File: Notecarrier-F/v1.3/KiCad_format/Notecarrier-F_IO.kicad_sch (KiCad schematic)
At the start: 2 parts, among them J10 CES-124-01-S-S, J9 CES-124-01-S-S

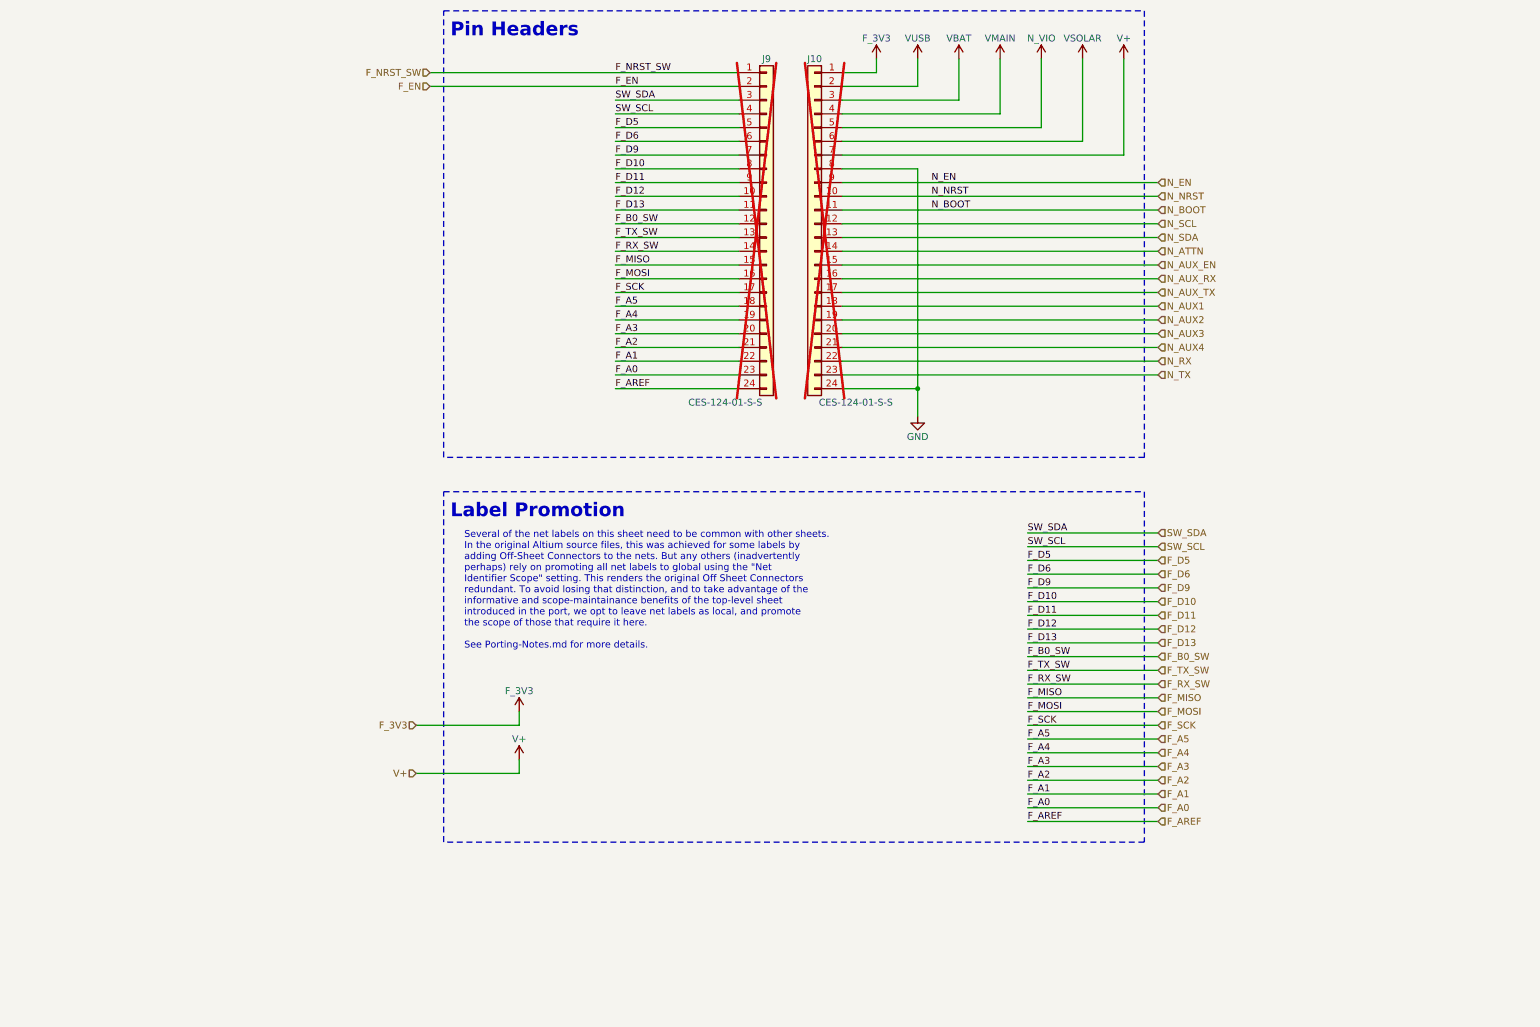
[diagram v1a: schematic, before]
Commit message: Notecarrier-F v1.3: KiCad 9 port from the release-day Altium sources
Replace the hand-made KiCad 7 port (which described v1.2, with a half-applied
v1.3 schematic delta and an ERRATA file) with a direct import of the v1.3
Altium project, recovered from the design archive's history: committed by the
design house on 2023-07-10, the day of the 2200-814 fabrication package, with a
Rev 11 schematic PDF byte-identical to the one published here. The Altium
sources are published alongside as Notecarrier-F/v1.3/Altium, as for v1.5.

The port follows the v1.5 procedure (KiCad 9.0.9 Altium project importer plus
scripted cleanup, scripts kept under documentation/scripts). All validation
gates pass: ERC 0, DRC 0 with schematic parity, BOM exact (94/94 vs
3000-653-002), placement 89/89 vs PNP-3000-653-002, gerber diff exact on outer
copper and masks with the reviewed inner-annulus/silk classes frozen as the
baseline, KiCanvas and RAG. The KiCad netlist was also matched pad by pad
against the nets carried by the Altium board file (0 conflicts).

J9/J10 are fitted per the released BOM (the 2023-08-31 re-save of the project
flips the variant to match); J11/R11/R12 are DNP. Design rules follow the
board's own Altium rule set (0.1 mm clearance). The old hand-port notes are
kept as History_Porting-Notes-hand-port.md because the harness README cites
them for the gerber-diff recipe; the RAG exclusion comment and the product
README are updated accordingly.

Co-Authored-By: Claude Fable 5.1 <noreply@anthropic.com>
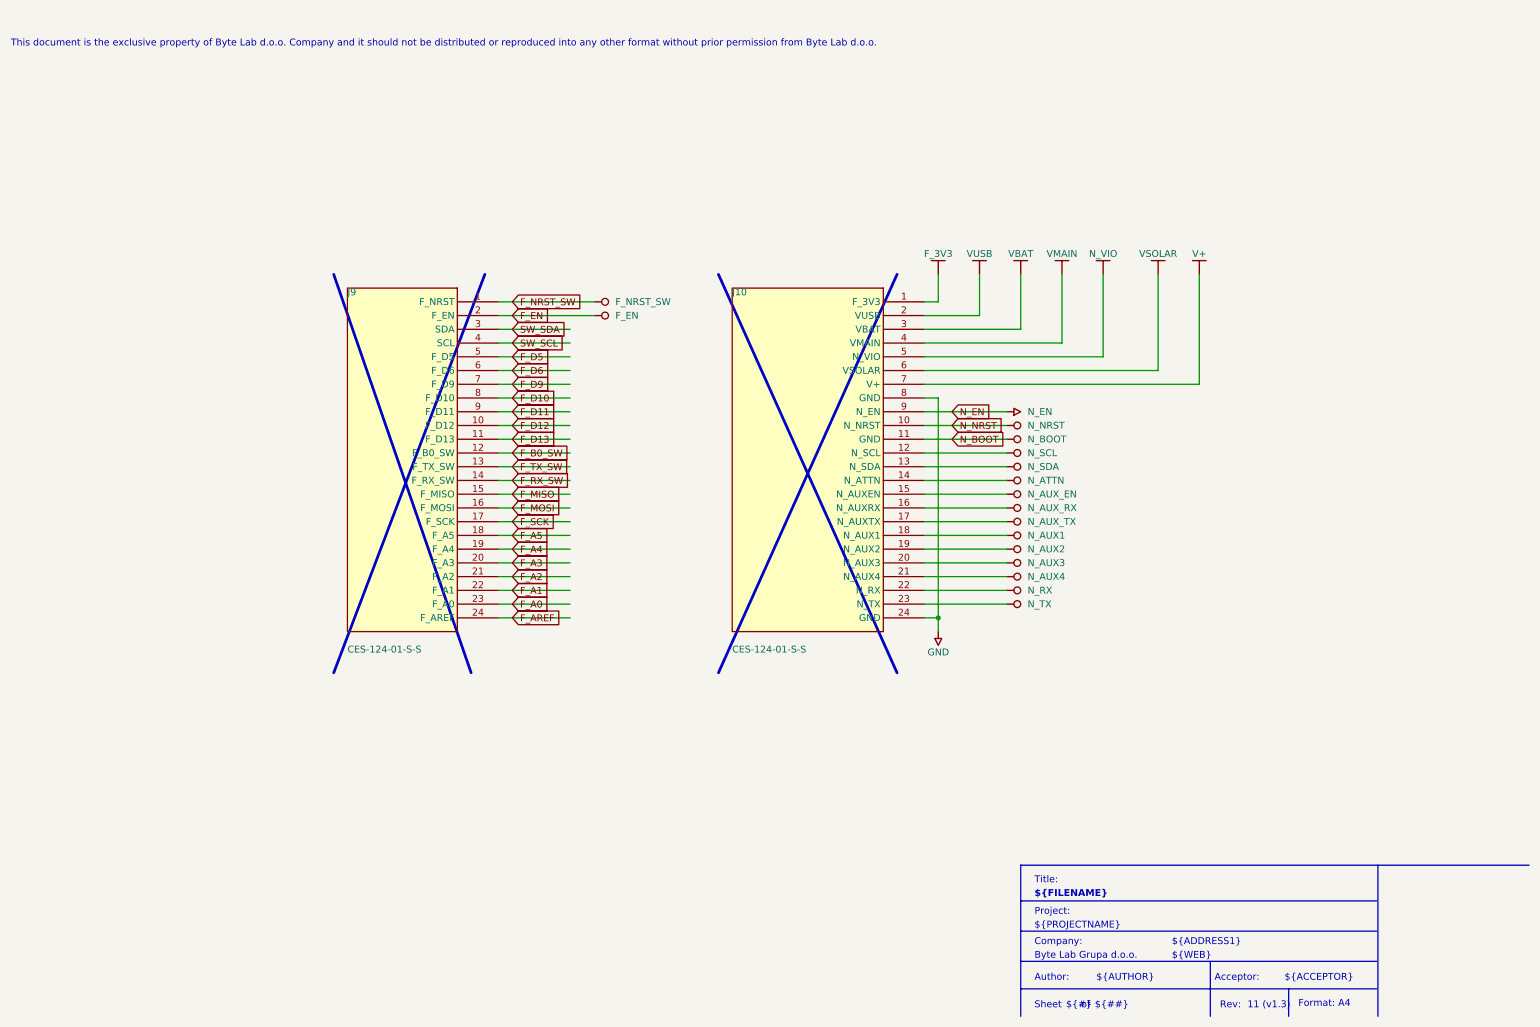
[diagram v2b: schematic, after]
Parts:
- removed J10, J9: CES-124-01-S-S, blues-kicad-lib:CES-124-01-S-S_Fv1.2, symbol Connector_Generic:Conn_01x24
- added J10: CES-124-01-S-S, Notecarrier-F-altium-import:CES-124-01-S-S, symbol n21-p2:root_0_SIDECON_N_n21-p2.SchLib_0
- added J9: CES-124-01-S-S, Notecarrier-F-altium-import:CES-124-01-S-S, symbol n21-p2:root_0_SIDECON_n21-p2.SchLib_0
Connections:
- net F_3V3: now also J10.1 (F_3V3)
- net F_A0: now also J9.23 (F_A0)
- net F_A1: now also J9.22 (F_A1)
- net F_A2: now also J9.21 (F_A2)
- net F_A3: now also J9.20 (F_A3)
- net F_A4: now also J9.19 (F_A4)
- net F_A5: now also J9.18 (F_A5)
- net F_AREF: now also J9.24 (F_AREF)
- net F_B0_SW: now also J9.12 (F_B0_SW)
- net F_D10: now also J9.8 (F_D10)
- net F_D11: now also J9.9 (F_D11)
- net F_D12: now also J9.10 (F_D12)
- net F_D13: now also J9.11 (F_D13)
- net F_D5: now also J9.5 (F_D5)
- net F_D6: now also J9.6 (F_D6)
- net F_D9: now also J9.7 (F_D9)
- net F_EN: now also J9.2 (F_EN)
- net F_MISO: now also J9.15 (F_MISO)
- net F_MOSI: now also J9.16 (F_MOSI)
- net F_NRST_SW: now also J9.1 (F_NRST)
- net F_RX_SW: now also J9.14 (F_RX_SW)
- net F_SCK: now also J9.17 (F_SCK)
- net F_TX_SW: now also J9.13 (F_TX_SW)
- net GND: now also J10.24 (GND), J10.8 (GND)
- net N_ATTN: now also J10.14 (N_ATTN)
- net N_AUX1: now also J10.18 (N_AUX1)
- net N_AUX2: now also J10.19 (N_AUX2)
- net N_AUX3: now also J10.20 (N_AUX3)
- net N_AUX4: now also J10.21 (N_AUX4)
- net N_AUX_EN: now also J10.15 (N_AUXEN)
- net N_AUX_RX: now also J10.16 (N_AUXRX)
- net N_AUX_TX: now also J10.17 (N_AUXTX)
- net N_BOOT: now also J10.11 (GND)
- net N_EN: now also J10.9 (N_EN)
- net N_NRST: now also J10.10 (N_NRST)
- net N_RX: now also J10.22 (N_RX)
- net N_SCL: now also J10.12 (N_SCL)
- net N_SDA: now also J10.13 (N_SDA)
- net N_TX: now also J10.23 (N_TX)
- net N_VIO: now also J10.5 (N_VIO)
- net SW_SCL: now also J9.4 (SCL)
- net SW_SDA: now also J9.3 (SDA)
- net V+: now also J10.7 (V+)
- net VBAT: now also J10.3 (VBAT)
- net VMAIN: now also J10.4 (VMAIN)
- net VSOLAR: now also J10.6 (VSOLAR)
- net VUSB: now also J10.2 (VUSB)
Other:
- note added: "${##}"
- note added: "${#}"
- note added: "${ACCEPTOR}"
- note added: "${ADDRESS1}"
- note added: "${AUTHOR}"
- note added: "${COMPANY}"
- note added: "${FILENAME}"
- note added: "${PROJECTNAME}"
- note added: "${REVISION}"
- note added: "${WEB}"
- note added: "Acceptor:"
- note added: "Author:"
- note added: "Company:"
- note added: "Format: A4"
- note added: "Project:"
- note added: "Rev:"
- note added: "Sheet"
- note added: "This document is the exclusive property of Byte Lab d.o.o. Company and it should not be distributed or reproduced into any other format without prior permission from Byte Lab d.o.o."
- note added: "Title:"
- note added: "of"
- note removed: "Label Promotion"
- note removed: "Pin Headers"
- note removed: "Several of the net labels on this sheet need to be common with other sheets. In the original Altium source files, this was achieved for some labels by adding Off-Sheet Connectors to the nets. But any others (inadvertently perhaps) rely on promoting all net labels to global using the "Net Identifier Scope" setting. This renders the original Off Sheet Connectors redundant. To avoid losing that dist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"
- company: (none) -> Byte Lab Grupa d.o.o.
